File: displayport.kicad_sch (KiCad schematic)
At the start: 25 parts, among them J11 DisplayPort, J12 DisplayPort, J9 DisplayPort, U14 FUSB340, U15 FUSB340, U16 TS3USB221RSER

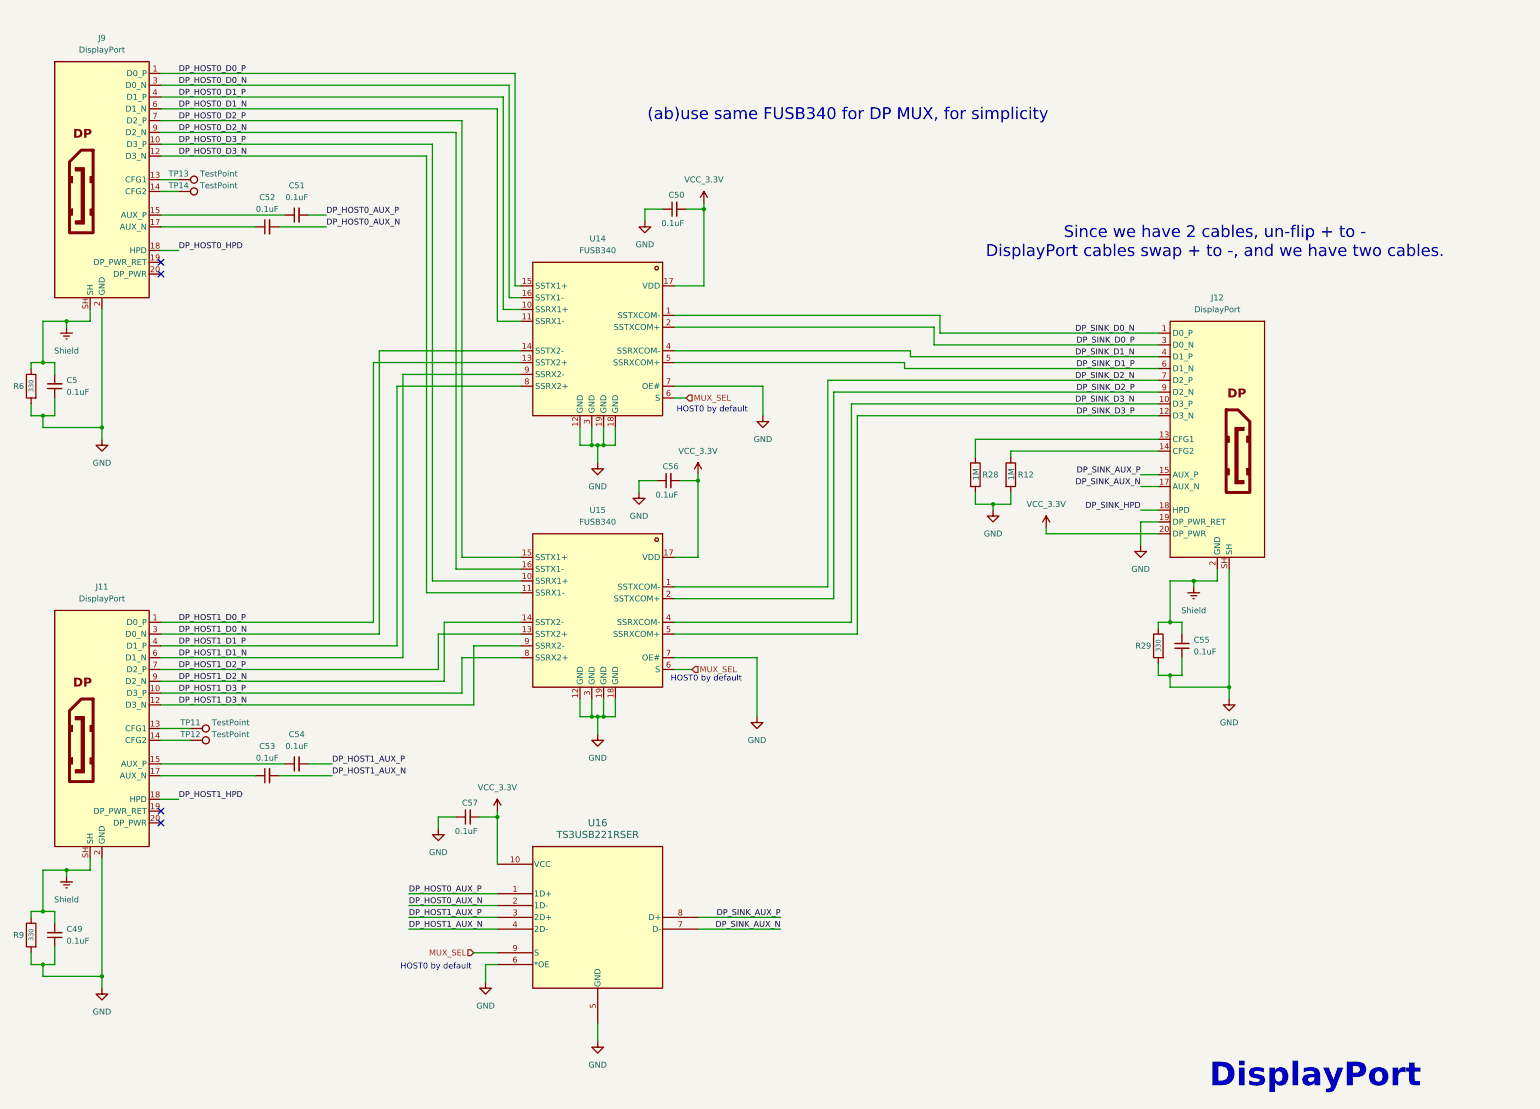
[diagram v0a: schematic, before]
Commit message: Add PI3DPX1203BZLEX DisplayPort redriver and start adding it to schematic
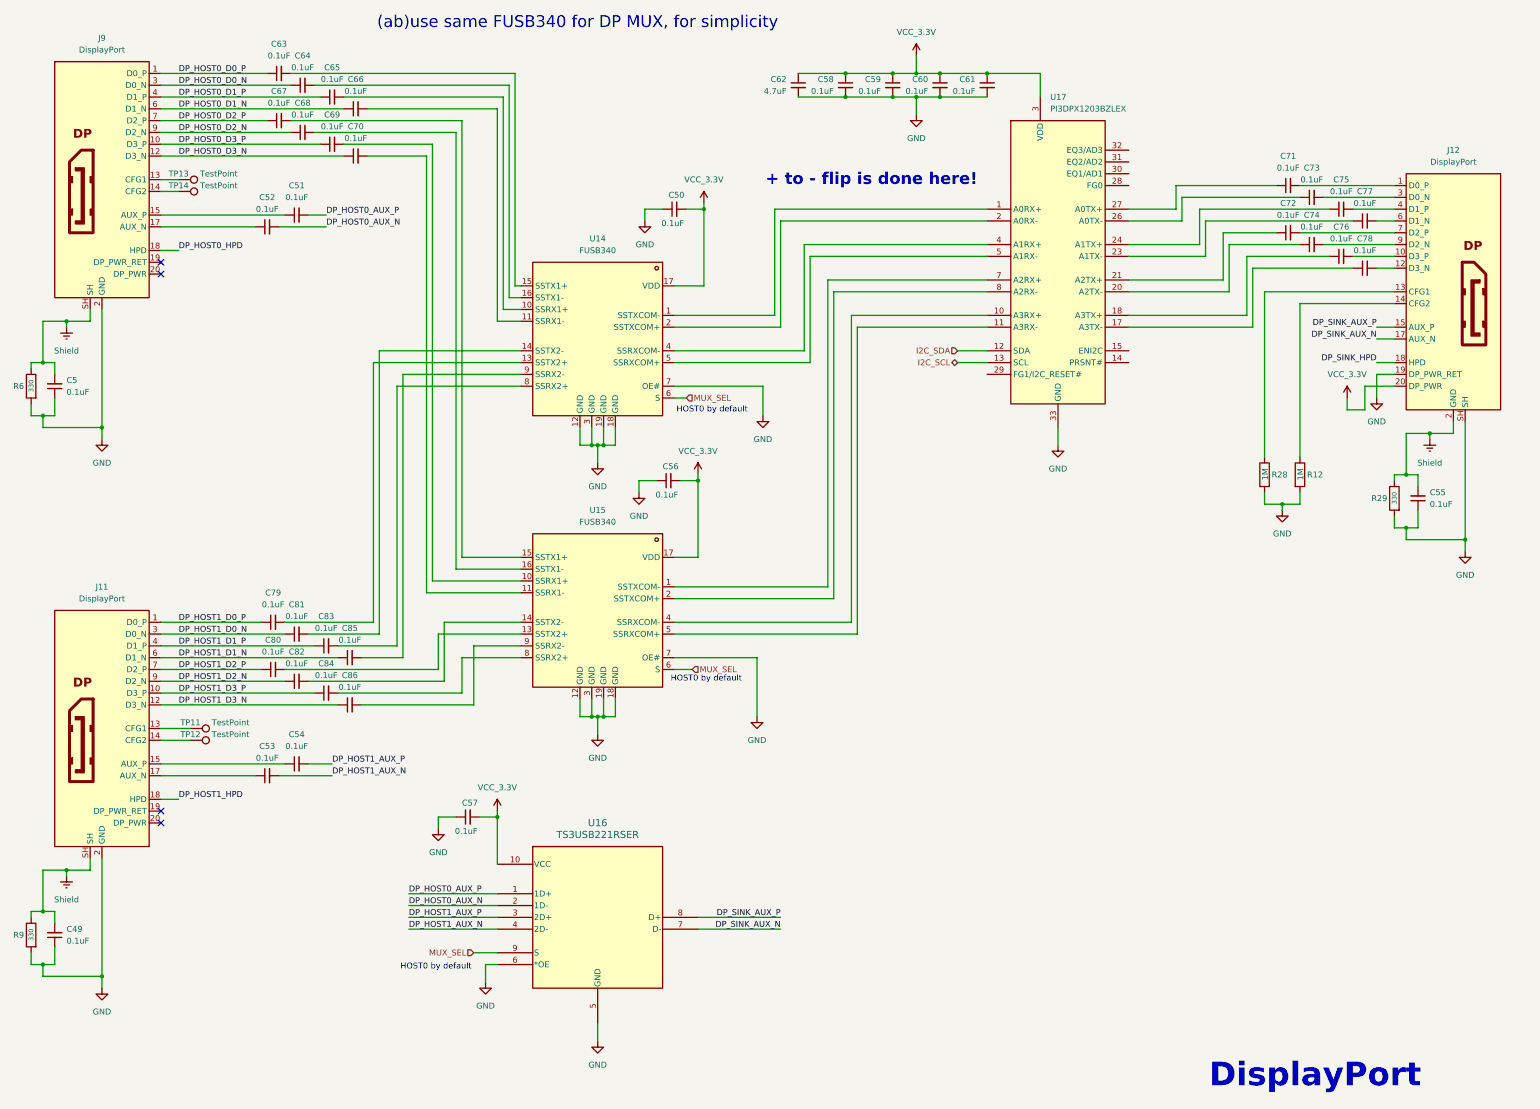
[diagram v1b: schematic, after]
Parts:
- added C58, C59, C60, C61: 0.1uF, Capacitor_SMD:C_0603_1608Metric, symbol Device:C_Small
- added C62: 4.7uF, Capacitor_SMD:C_0603_1608Metric, symbol Device:C_Small
- added C63, C64, C65, C66, C67, C68, C69, C70, C71, C72, C73, C74, C75, C76, C77, C78, C79, C80, C81, C82, C83, C84, C85, C86: 0.1uF, Capacitor_SMD:C_0402_1005Metric, symbol Device:C_Small
- added U17: PI3DPX1203BZLEX, hubble:QFN40P300X600X80-33N, symbol hubble:PI3DPX1203BZLEX
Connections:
- net DP_HOST0_D0_N: now also C64.1; no longer U14.16 (SSTX1-)
- net DP_HOST0_D0_P: now also C63.1; no longer U14.15 (SSTX1+)
- net DP_HOST0_D1_N: now also C66.1; no longer U14.11 (SSRX1-)
- net DP_HOST0_D1_P: now also C65.1; no longer U14.10 (SSRX1+)
- net DP_HOST0_D2_N: now also C68.1; no longer U15.16 (SSTX1-)
- net DP_HOST0_D2_P: now also C67.1; no longer U15.15 (SSTX1+)
- net DP_HOST0_D3_N: now also C70.1; no longer U15.11 (SSRX1-)
- net DP_HOST0_D3_P: now also C69.1; no longer U15.10 (SSRX1+)
- net DP_HOST1_D0_N: now also C81.1; no longer U14.14 (SSTX2-)
- net DP_HOST1_D0_P: now also C79.1; no longer U14.13 (SSTX2+)
- net DP_HOST1_D1_N: now also C85.1; no longer U14.9 (SSRX2-)
- net DP_HOST1_D1_P: now also C83.1; no longer U14.8 (SSRX2+)
- net DP_HOST1_D2_N: now also C82.1; no longer U15.14 (SSTX2-)
- net DP_HOST1_D2_P: now also C80.1; no longer U15.13 (SSTX2+)
- net DP_HOST1_D3_N: now also C86.1; no longer U15.9 (SSRX2-)
- net DP_HOST1_D3_P: now also C84.1; no longer U15.8 (SSRX2+)
- net GND: now also C58.2, C59.2, C60.2, C61.2, C62.2, U17.33 (GND)
- net VCC_3.3V: now also C58.1, C59.1, C60.1, C61.1, C62.1, U17.19 (VDD_4), U17.22 (VDD_5), U17.25 (VDD_6), U17.3 (VDD), U17.6 (VDD_2), U17.9 (VDD_3)
- net DP_SINK_D0_N: no longer names the net of U14.1 (SSTXCOM-)
- net DP_SINK_D0_N: now also U17.1 (A0RX+); no longer J12.1 (D0_P)
- net DP_SINK_D0_P: no longer names the net of U14.2 (SSTXCOM+)
- net DP_SINK_D0_P: now also U17.2 (A0RX-); no longer J12.3 (D0_N)
- net DP_SINK_D1_N: no longer names the net of U14.4 (SSRXCOM-)
- net DP_SINK_D1_N: now also U17.4 (A1RX+); no longer J12.4 (D1_P)
- net DP_SINK_D1_P: no longer names the net of U14.5 (SSRXCOM+)
- net DP_SINK_D1_P: now also U17.5 (A1RX-); no longer J12.6 (D1_N)
- net DP_SINK_D2_N: no longer names the net of U15.1 (SSTXCOM-)
- net DP_SINK_D2_N: now also U17.7 (A2RX+); no longer J12.7 (D2_P)
- net DP_SINK_D2_P: no longer names the net of U15.2 (SSTXCOM+)
- net DP_SINK_D2_P: now also U17.8 (A2RX-); no longer J12.9 (D2_N)
- net DP_SINK_D3_N: no longer names the net of U15.4 (SSRXCOM-)
- net DP_SINK_D3_N: now also U17.10 (A3RX+); no longer J12.10 (D3_P)
- net DP_SINK_D3_P: no longer names the net of U15.5 (SSRXCOM+)
- net DP_SINK_D3_P: now also U17.11 (A3RX-); no longer J12.12 (D3_N)
- new net: C78.1, U17.17 (A3TX-)
- new net: C76.1, U17.18 (A3TX+)
- new net: C74.1, U17.20 (A2TX-)
- new net: C72.1, U17.21 (A2TX+)
- new net: C77.1, U17.23 (A1TX-)
- new net: C75.1, U17.24 (A1TX+)
- new net: C73.1, U17.26 (A0TX-)
- new net: C71.1, U17.27 (A0TX+)
- new net: C85.2, U14.9 (SSRX2-)
- new net: C82.2, U15.14 (SSTX2-)
- new net: C69.2, U15.10 (SSRX1+)
- new net: C70.2, U15.11 (SSRX1-)
- new net: C80.2, U15.13 (SSTX2+)
- new net: C67.2, U15.15 (SSTX1+)
- new net: C68.2, U15.16 (SSTX1-)
- new net: C84.2, U15.8 (SSRX2+)
- new net: C86.2, U15.9 (SSRX2-)
- new net: C81.2, U14.14 (SSTX2-)
- new net: C63.2, U14.15 (SSTX1+)
- new net: C65.2, U14.10 (SSRX1+)
- new net: C66.2, U14.11 (SSRX1-)
- new net: C79.2, U14.13 (SSTX2+)
- new net: C64.2, U14.16 (SSTX1-)
- new net: C83.2, U14.8 (SSRX2+)
- new net: C75.2, J12.4 (D1_P)
- new net: C73.2, J12.3 (D0_N)
- new net: C71.2, J12.1 (D0_P)
- new net: C76.2, J12.10 (D3_P)
- new net: C78.2, J12.12 (D3_N)
- new net: C77.2, J12.6 (D1_N)
- new net: C72.2, J12.7 (D2_P)
- new net: C74.2, J12.9 (D2_N)
- new net I2C_SCL: U17.13 (SCL)
- new net I2C_SDA: U17.12 (SDA)
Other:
- note added: "+ to - flip is done here!"
- note removed: "Since we have 2 cables, un-flip + to - DisplayPort cables swap + to -, and we have two cables."
- moved on the sheet: C55, J12, R12, R28, R29

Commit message: Change all high-speed decoupling caps to 0402s
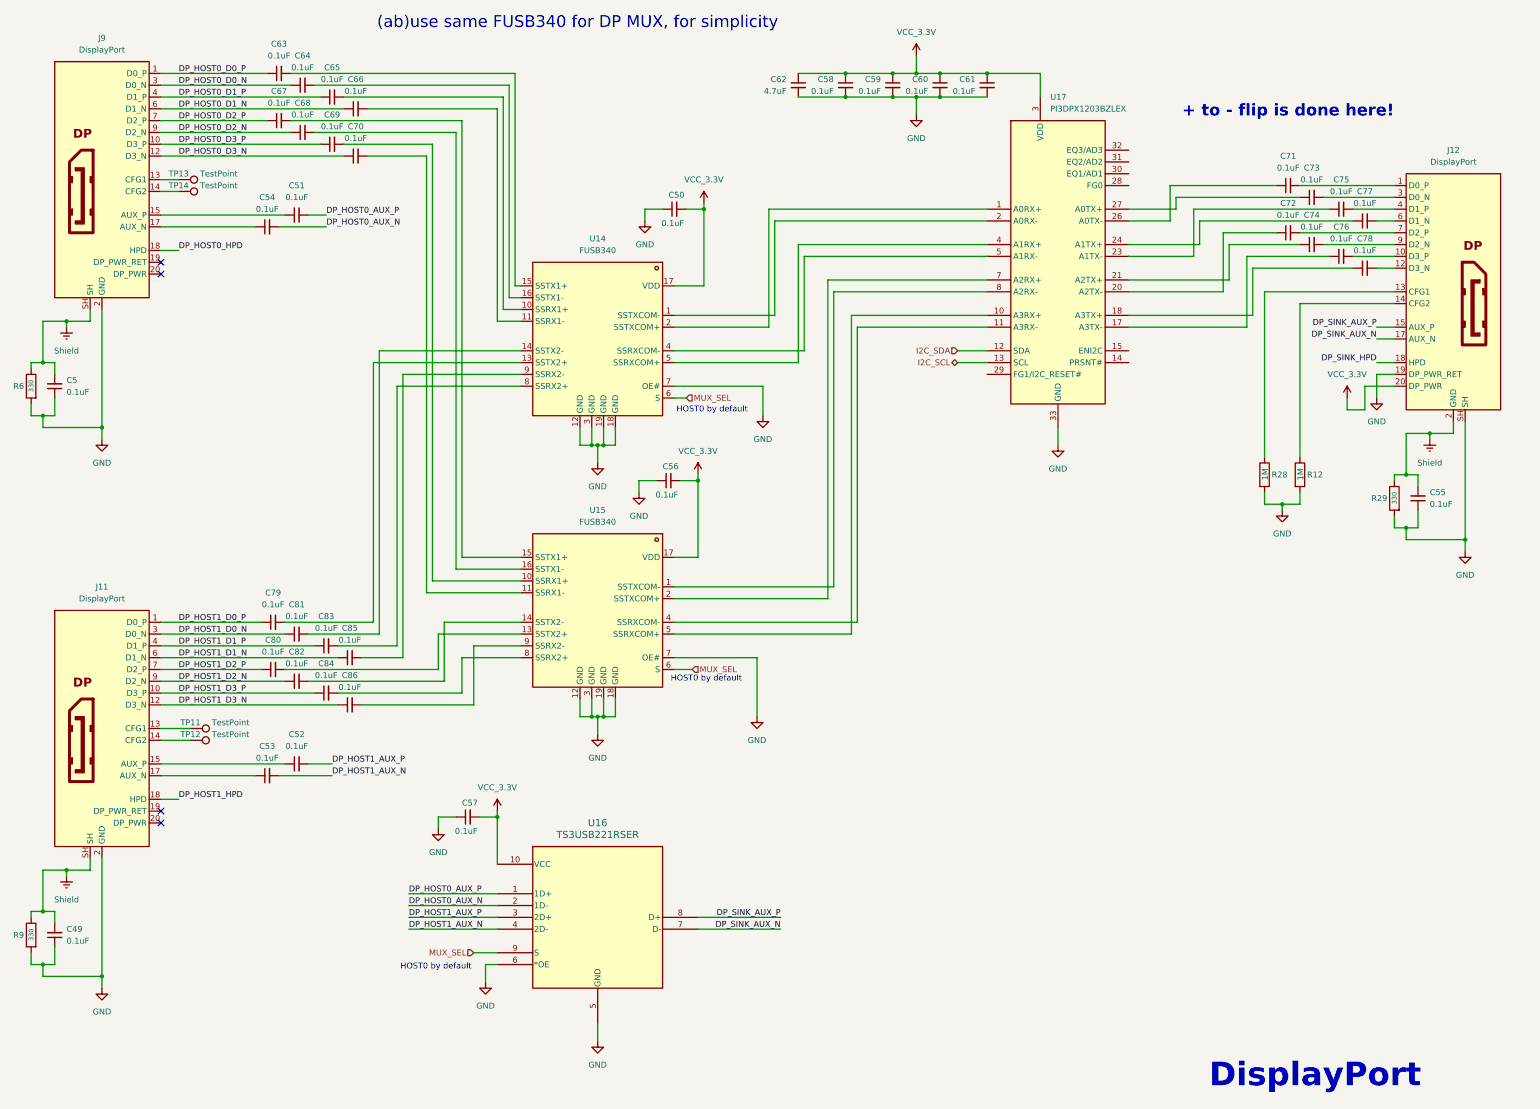
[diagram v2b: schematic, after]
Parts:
- C51, C52, C53, C54: footprint Capacitor_SMD:C_0603_1608Metric -> Capacitor_SMD:C_0402_1005Metric
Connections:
- net DP_HOST0_AUX_N: now also C54.2; no longer C52.2
- net DP_HOST1_AUX_P: now also C52.2; no longer C54.2
- net at U17.1 (A0RX+): now also U14.2 (SSTXCOM+); no longer U14.1 (SSTXCOM-)
- net at U17.10 (A3RX+): now also U15.5 (SSRXCOM+); no longer U15.4 (SSRXCOM-)
- net at U17.11 (A3RX-): now also U15.4 (SSRXCOM-); no longer U15.5 (SSRXCOM+)
- net at U17.17 (A3TX-): now also C76.1; no longer C78.1
- net at U17.18 (A3TX+): now also C78.1; no longer C76.1
- net at U17.2 (A0RX-): now also U14.1 (SSTXCOM-); no longer U14.2 (SSTXCOM+)
- net at U17.20 (A2TX-): now also C72.1; no longer C74.1
- net at U17.21 (A2TX+): now also C74.1; no longer C72.1
- net at U17.23 (A1TX-): now also C75.1; no longer C77.1
- net at U17.24 (A1TX+): now also C77.1; no longer C75.1
- net at U17.26 (A0TX-): now also C71.1; no longer C73.1
- net at U17.27 (A0TX+): now also C73.1; no longer C71.1
- net at U17.4 (A1RX+): now also U14.5 (SSRXCOM+); no longer U14.4 (SSRXCOM-)
- net at U17.5 (A1RX-): now also U14.4 (SSRXCOM-); no longer U14.5 (SSRXCOM+)
- net at U17.7 (A2RX+): now also U15.2 (SSTXCOM+); no longer U15.1 (SSTXCOM-)
- net at U17.8 (A2RX-): now also U15.1 (SSTXCOM-); no longer U15.2 (SSTXCOM+)
- net at J11.15 (AUX_P): now also C52.1; no longer C54.1
- net at J9.17 (AUX_N): now also C54.1; no longer C52.1

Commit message: Wiring up DisplayPort HPD signals
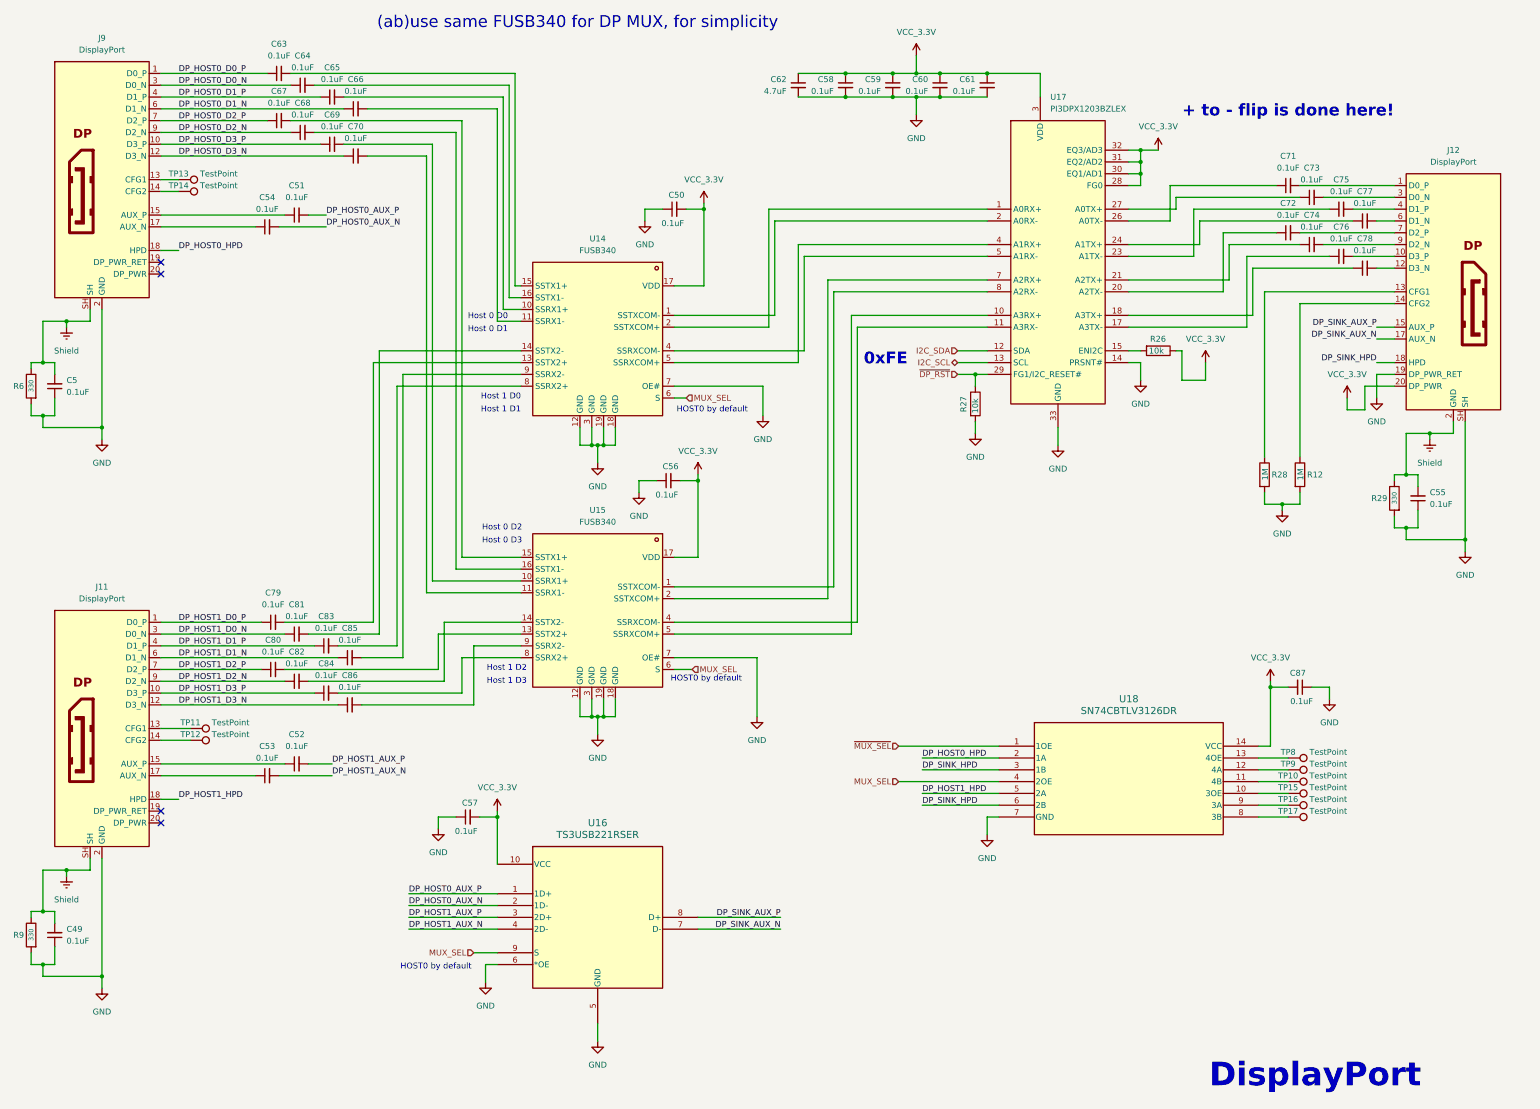
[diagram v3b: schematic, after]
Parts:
- added C87: 0.1uF, Capacitor_SMD:C_0603_1608Metric, symbol Device:C_Small
- added R26, R27: 10k, Resistor_SMD:R_0603_1608Metric, symbol Device:R
- added TP10, TP15, TP16, TP17, TP8, TP9: TestPoint, TestPoint:TestPoint_Pad_1.0x1.0mm, symbol Connector:TestPoint
- added U18: SN74CBTLV3126DR, hubble:D14, symbol hubble:SN74CBTLV3126DR
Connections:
- net DP_HOST0_HPD: now also U18.2 (1A)
- net DP_HOST1_HPD: now also U18.5 (2A)
- net DP_SINK_HPD: now also U18.3 (1B), U18.6 (2B)
- net GND: now also U17.14 (PRSNT#), C87.1, R27.2, U18.7 (GND)
- net MUX_SEL: now also U18.4 (2OE)
- net VCC_3.3V: now also U17.28 (FG0), U17.30 (EQ1/AD1), U17.31 (EQ2/AD2), U17.32 (EQ3/AD3), C87.2, R26.1, U18.14 (VCC)
- net at U17.15 (ENI2C): now also R26.2
- net ~{DP_RST}: now reaches U17.29 (FG1/I2C_RESET#)
- net ~{DP_RST}: now also R27.1
- new net: TP9.1, U18.12 (4A)
- new net: TP17.1, U18.8 (3B)
- new net: TP15.1, U18.10 (3OE)
- new net: TP16.1, U18.9 (3A)
- new net: TP8.1, U18.13 (4OE)
- new net: TP10.1, U18.11 (4B)
- new net ~{MUX_SEL}: U18.1 (1OE)
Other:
- note added: "0xFE"
- note added: "Host 0 D0"
- note added: "Host 0 D1"
- note added: "Host 0 D2"
- note added: "Host 0 D3"
- note added: "Host 1 D0"
- note added: "Host 1 D1"
- note added: "Host 1 D2"
- note added: "Host 1 D3"
